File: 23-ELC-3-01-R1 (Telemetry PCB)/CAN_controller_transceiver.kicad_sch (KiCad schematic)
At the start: 23 parts, among them U7 MCP2515-xSO, U8 SN65HVD230, Y1 16 MHz

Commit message: Finished CAN circuits probably
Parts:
- renumbered C21 to C?, C18 to C?, C19 to C?, C20 to C?, C22 to C?, JP1 to JP?, JP2 to JP?, JP3 to JP?, JP4 to JP?, R28 to R?, R30 to R?, R29 to R?, R31 to R?, R32 to R?, TP12 to TP?, TP11 to TP?, TP10 to TP?, TP9 to TP?, TP13 to TP?, TP14 to TP?, U7 to U?, U8 to U?, Y1 to Y?
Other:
- note added: "TODO: Check if RESET and INT need pull ups"

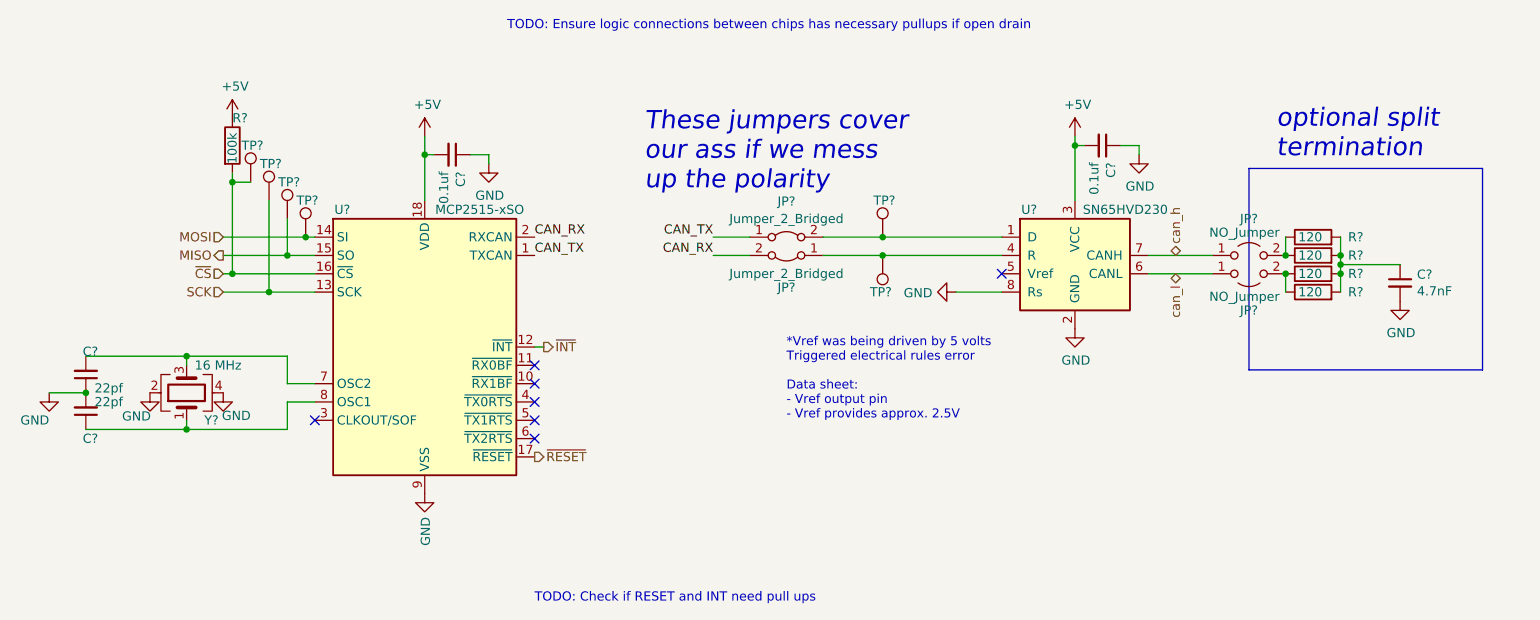
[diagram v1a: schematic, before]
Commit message: Schematic finished, working on layout
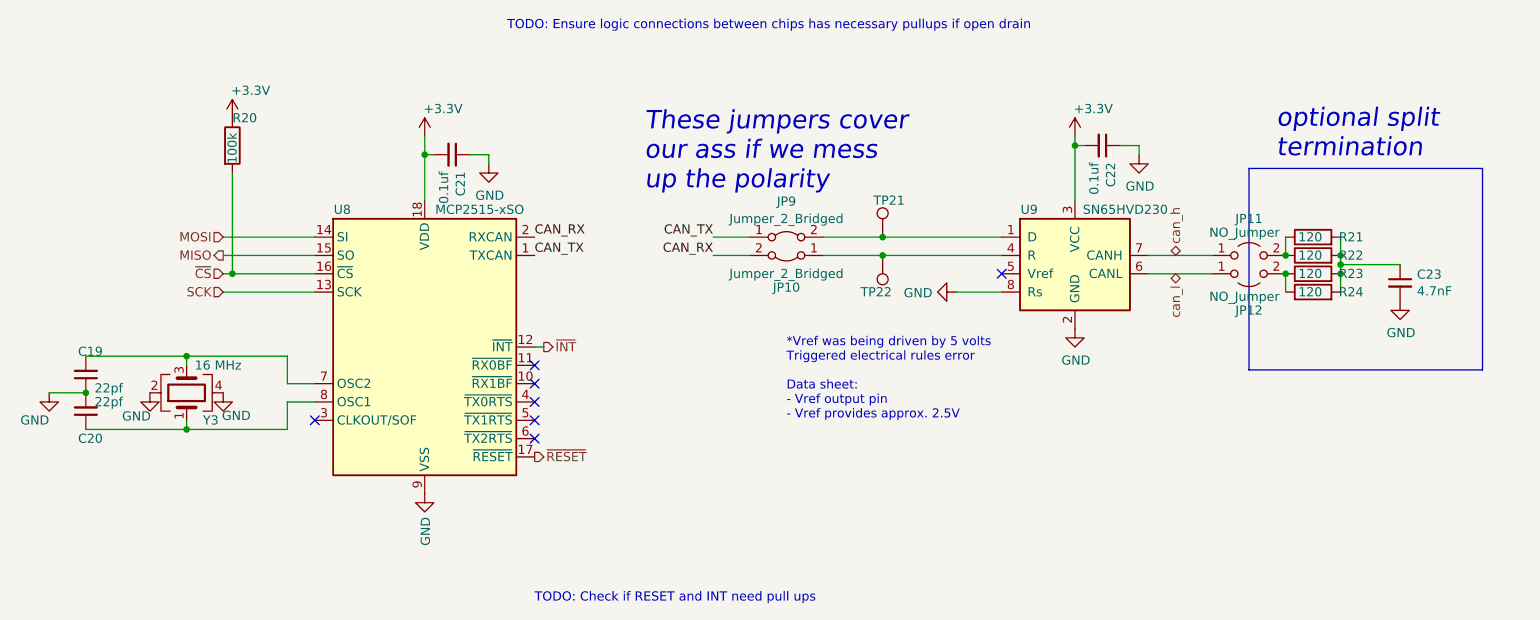
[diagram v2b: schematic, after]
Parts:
- removed TP? (x4): TestPoint, TestPoint:TestPoint_THTPad_D1.0mm_Drill0.5mm, symbol Connector:TestPoint
- JP11, JP12: renamed from JP?; footprint Connector_PinHeader_2.54mm:PinHeader_1x02_P2.54mm_Vertical -> Jumper:SolderJumper-2_P1.3mm_Open_RoundedPad1.0x1.5mm
- gave numbers to parts that had none: 17
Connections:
- net +5V renamed +3V3

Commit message: First draft of layout
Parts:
- renumbered C20 to C10, C21 to C11, C22 to C12, C23 to C13, C19 to C9, JP9 to JP1, JP10 to JP2, JP11 to JP3, JP12 to JP4, R20 to R10, R21 to R11, R22 to R12, R23 to R13, R24 to R14, TP22 to TP10, TP21 to TP9, U8 to U4, U9 to U5, Y3 to Y1
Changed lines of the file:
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@@
   (symbol (lib_id "Device:C_Small") (at 177.8 91.44 270)
     (in_bom yes) (on_board yes)
-    (property "Reference" "C22" (id 0) (at 178.9684 93.7768 0)
+    (property "Reference" "C12" (id 0) (at 178.9684 93.7768 0)
       (effects (font (size 1.27 1.27)) (justify left))
     )
@@
   (symbol (lib_id "power:GND") (at 173.99 116.84 0)
     (in_bom yes) (on_board yes)
-    (property "Reference" "#PWR075" (id 0) (at 173.99 123.19 0)
+    (property "Reference" "#PWR051" (id 0) (at 173.99 123.19 0)
       (effects (font (size 1.27 1.27)) hide)
     )
@@
   (symbol (lib_id "power:GND") (at 182.88 92.71 0)
     (in_bom yes) (on_board yes)
-    (property "Reference" "#PWR076" (id 0) (at 182.88 99.06 0)
+    (property "Reference" "#PWR052" (id 0) (at 182.88 99.06 0)
       (effects (font (size 1.27 1.27)) hide)
     )
@@
   (symbol (lib_id "power:GND") (at 157.48 111.76 270)
     (in_bom yes) (on_board yes)
-    (property "Reference" "#PWR073" (id 0) (at 151.13 111.76 0)
+    (property "Reference" "#PWR049" (id 0) (at 151.13 111.76 0)
       (effects (font (size 1.27 1.27)) hide)
     )
@@
   (symbol (lib_id "Interface_CAN_LIN:MCP2515-xSO") (at 83.82 119.38 0)
     (in_bom yes) (on_board yes)
-    (property "Reference" "U8" (id 0) (at 72.39 100.33 0))
+    (property "Reference" "U4" (id 0) (at 72.39 100.33 0))
     (property "Value" "MCP2515-xSO" (id 1) (at 91.44 100.33 0))
     (property "Footprint" "Package_SO:SOIC-18W_7.5x11.6mm_P1.27mm" (id 2) (at 83.82 142.24 0)
@@
   (symbol (lib_id "Interface_CAN_LIN:SN65HVD230") (at 173.99 106.68 0)
     (in_bom yes) (on_board yes)
-    (property "Reference" "U9" (id 0) (at 167.64 100.33 0))
+    (property "Reference" "U5" (id 0) (at 167.64 100.33 0))
     (property "Value" "SN65HVD230" (id 1) (at 180.975 100.33 0))
     (property "Footprint" "Package_SO:SOIC-8_3.9x4.9mm_P1.27mm" (id 2) (at 173.99 119.38 0)
@@
   (symbol (lib_id "Device:Crystal_GND24") (at 50.8 125.73 90)
     (in_bom yes) (on_board yes)
-    (property "Reference" "Y3" (id 0) (at 55.245 129.54 90)
+    (property "Reference" "Y1" (id 0) (at 55.245 129.54 90)
       (effects (font (size 1.27 1.27)) (justify left))
     )
@@
   (symbol (lib_id "power:GND") (at 83.82 139.7 0)
     (in_bom yes) (on_board yes)
-    (property "Reference" "#PWR071" (id 0) (at 83.82 146.05 0)
+    (property "Reference" "#PWR047" (id 0) (at 83.82 146.05 0)
       (effects (font (size 1.27 1.27)) hide)
     )
@@
   (symbol (lib_id "power:GND") (at 45.72 125.73 0)
     (in_bom yes) (on_board yes)
-    (property "Reference" "#PWR067" (id 0) (at 45.72 132.08 0)
+    (property "Reference" "#PWR043" (id 0) (at 45.72 132.08 0)
       (effects (font (size 1.27 1.27)) hide)
     )
@@
   (symbol (lib_id "power:GND") (at 55.88 125.73 0)
     (in_bom yes) (on_board yes)
-    (property "Reference" "#PWR068" (id 0) (at 55.88 132.08 0)
+    (property "Reference" "#PWR044" (id 0) (at 55.88 132.08 0)
       (effects (font (size 1.27 1.27)) hide)
     )
@@
   (symbol (lib_id "Device:C_Small") (at 36.83 123.19 180)
     (in_bom yes) (on_board yes)
-    (property "Reference" "C19" (id 0) (at 37.465 120.015 0))
+    (property "Reference" "C9" (id 0) (at 37.465 120.015 0))
     (property "Value" "22pf" (id 1) (at 40.005 125.095 0))
     (property "Footprint" "Capacitor_SMD:C_0603_1608Metric_Pad1.08x0.95mm_HandSolder" (id 2) (at 36.83 123.19 0)
@@
   (symbol (lib_id "Device:C_Small") (at 36.83 128.27 180)
     (in_bom yes) (on_board yes)
-    (property "Reference" "C20" (id 0) (at 37.465 132.08 0))
+    (property "Reference" "C10" (id 0) (at 37.465 132.08 0))
     (property "Value" "22pf" (id 1) (at 40.005 127 0))
     (property "Footprint" "Capacitor_SMD:C_0603_1608Metric_Pad1.08x0.95mm_HandSolder" (id 2) (at 36.83 128.27 0)
@@
   (symbol (lib_id "power:GND") (at 31.75 125.73 0)
     (in_bom yes) (on_board yes)
-    (property "Reference" "#PWR066" (id 0) (at 31.75 132.08 0)
+    (property "Reference" "#PWR042" (id 0) (at 31.75 132.08 0)
       (effects (font (size 1.27 1.27)) hide)
     )
@@
   (symbol (lib_id "Device:C_Small") (at 87.63 92.71 270)
     (in_bom yes) (on_board yes)
-    (property "Reference" "C21" (id 0) (at 88.7984 95.0468 0)
+    (property "Reference" "C11" (id 0) (at 88.7984 95.0468 0)
       (effects (font (size 1.27 1.27)) (justify left))
     )
@@
   (symbol (lib_id "power:GND") (at 92.71 93.98 0)
     (in_bom yes) (on_board yes)
-    (property "Reference" "#PWR072" (id 0) (at 92.71 100.33 0)
+    (property "Reference" "#PWR048" (id 0) (at 92.71 100.33 0)
       (effects (font (size 1.27 1.27)) hide)
     )
@@
   (symbol (lib_id "Device:R") (at 57.15 91.44 0)
     (in_bom yes) (on_board yes)
-    (property "Reference" "R20" (id 0) (at 57.15 87.63 0)
+    (property "Reference" "R10" (id 0) (at 57.15 87.63 0)
       (effects (font (size 1.27 1.27)) (justify left))
     )
@@
   (symbol (lib_id "Connector:TestPoint") (at 147.32 104.14 0)
     (in_bom yes) (on_board yes)
-    (property "Reference" "TP21" (id 0) (at 146.05 99.06 0)
+    (property "Reference" "TP9" (id 0) (at 146.05 99.06 0)
       (effects (font (size 1.27 1.27)) (justify left))
     )
@@
   (symbol (lib_id "Connector:TestPoint") (at 147.32 106.68 180)
     (in_bom yes) (on_board yes)
-    (property "Reference" "TP22" (id 0) (at 148.59 111.76 0)
+    (property "Reference" "TP10" (id 0) (at 148.59 111.76 0)
       (effects (font (size 1.27 1.27)) (justify left))
     )
@@
   (symbol (lib_id "Jumper:Jumper_2_Bridged") (at 133.985 104.14 0)
     (in_bom yes) (on_board yes)
-    (property "Reference" "JP9" (id 0) (at 133.985 99.187 0))
+    (property "Reference" "JP1" (id 0) (at 133.985 99.187 0))
     (property "Value" "Jumper_2_Bridged" (id 1) (at 133.985 101.6 0))
     (property "Footprint" "Jumper:SolderJumper-2_P1.3mm_Bridged_RoundedPad1.0x1.5mm" (id 2) (at 133.985 104.14 0)
@@
   (symbol (lib_id "Jumper:Jumper_2_Bridged") (at 133.985 106.68 180)
     (in_bom yes) (on_board yes)
-    (property "Reference" "JP10" (id 0) (at 133.985 111.125 0))
+    (property "Reference" "JP2" (id 0) (at 133.985 111.125 0))
     (property "Value" "Jumper_2_Bridged" (id 1) (at 133.985 109.22 0))
     (property "Footprint" "Jumper:SolderJumper-2_P1.3mm_Bridged_RoundedPad1.0x1.5mm" (id 2) (at 133.985 106.68 0)
@@
   (symbol (lib_id "Jumper:Jumper_2_Open") (at 198.12 106.68 0)
     (in_bom yes) (on_board yes)
-    (property "Reference" "JP11" (id 0) (at 198.12 101.6 0))
+    (property "Reference" "JP3" (id 0) (at 198.12 101.6 0))
     (property "Value" "NO_Jumper" (id 1) (at 197.485 103.505 0))
     (property "Footprint" "Jumper:SolderJumper-2_P1.3mm_Open_RoundedPad1.0x1.5mm" (id 2) (at 198.12 106.68 0)
@@
   (symbol (lib_id "Jumper:Jumper_2_Open") (at 198.12 109.22 0) (mirror x)
     (in_bom yes) (on_board yes)
-    (property "Reference" "JP12" (id 0) (at 198.12 114.3 0))
+    (property "Reference" "JP4" (id 0) (at 198.12 114.3 0))
     (property "Value" "NO_Jumper" (id 1) (at 197.485 112.395 0))
     (property "Footprint" "Jumper:SolderJumper-2_P1.3mm_Open_RoundedPad1.0x1.5mm" (id 2) (at 198.12 109.22 0)
@@
   (symbol (lib_id "Device:C_Small") (at 219.075 110.49 0)
     (in_bom yes) (on_board yes)
-    (property "Reference" "C23" (id 0) (at 221.4118 109.3216 0)
+    (property "Reference" "C13" (id 0) (at 221.4118 109.3216 0)
       (effects (font (size 1.27 1.27)) (justify left))
     )
@@
   (symbol (lib_id "Device:R") (at 207.01 106.68 90)
     (in_bom yes) (on_board yes)
-    (property "Reference" "R22" (id 0) (at 213.995 106.68 90)
+    (property "Reference" "R12" (id 0) (at 213.995 106.68 90)
       (effects (font (size 1.27 1.27)) (justify left))
     )
@@
   (symbol (lib_id "Device:R") (at 207.01 104.14 90)
     (in_bom yes) (on_board yes)
-    (property "Reference" "R21" (id 0) (at 213.995 104.14 90)
+    (property "Reference" "R11" (id 0) (at 213.995 104.14 90)
       (effects (font (size 1.27 1.27)) (justify left))
     )
@@
   (symbol (lib_id "Device:R") (at 207.01 109.22 90)
     (in_bom yes) (on_board yes)
-    (property "Reference" "R23" (id 0) (at 213.995 109.22 90)
+    (property "Reference" "R13" (id 0) (at 213.995 109.22 90)
       (effects (font (size 1.27 1.27)) (justify left))
     )
@@
   (symbol (lib_id "Device:R") (at 207.01 111.76 90)
     (in_bom yes) (on_board yes)
-    (property "Reference" "R24" (id 0) (at 213.995 111.76 90)
+    (property "Reference" "R14" (id 0) (at 213.995 111.76 90)
       (effects (font (size 1.27 1.27)) (justify left))
     )
@@
   (symbol (lib_id "power:GND") (at 219.075 113.03 0)
     (in_bom yes) (on_board yes)
-    (property "Reference" "#PWR077" (id 0) (at 219.075 119.38 0)
+    (property "Reference" "#PWR053" (id 0) (at 219.075 119.38 0)
       (effects (font (size 1.27 1.27)) hide)
     )
@@
   (symbol (lib_id "power:+3.3V") (at 57.15 87.63 0)
     (in_bom yes) (on_board yes)
-    (property "Reference" "#PWR069" (id 0) (at 57.15 91.44 0)
+    (property "Reference" "#PWR045" (id 0) (at 57.15 91.44 0)
       (effects (font (size 1.27 1.27)) hide)
     )
@@
   (symbol (lib_id "power:+3.3V") (at 83.82 90.17 0)
     (in_bom yes) (on_board yes)
-    (property "Reference" "#PWR070" (id 0) (at 83.82 93.98 0)
+    (property "Reference" "#PWR046" (id 0) (at 83.82 93.98 0)
       (effects (font (size 1.27 1.27)) hide)
     )
@@
   (symbol (lib_id "power:+3.3V") (at 173.99 90.17 0)
     (in_bom yes) (on_board yes)
-    (property "Reference" "#PWR074" (id 0) (at 173.99 93.98 0)
-      (effects (font (size 1.27 1.27)) hide)
-    )
+    (property "Reference" "#PWR050" (id 0) (at 173.99 93.98 0)
+      (effects (font (size 1.27 1.27)) hide)
+    )
